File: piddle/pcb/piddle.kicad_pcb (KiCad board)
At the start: 2 copper layers, 139.2 x 138.5 mm, 88 parts, among them J1 Conn_01x03_Socket, J10 Conn_01x03_Socket, J11 Conn_01x03_Socket, J12 Conn_01x03_Socket, J13 Conn_01x03_Socket, J14 Conn_01x03_Socket, J15 Conn_01x03_Socket, J16 infrared receiver, J17 5v, J18 3v3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

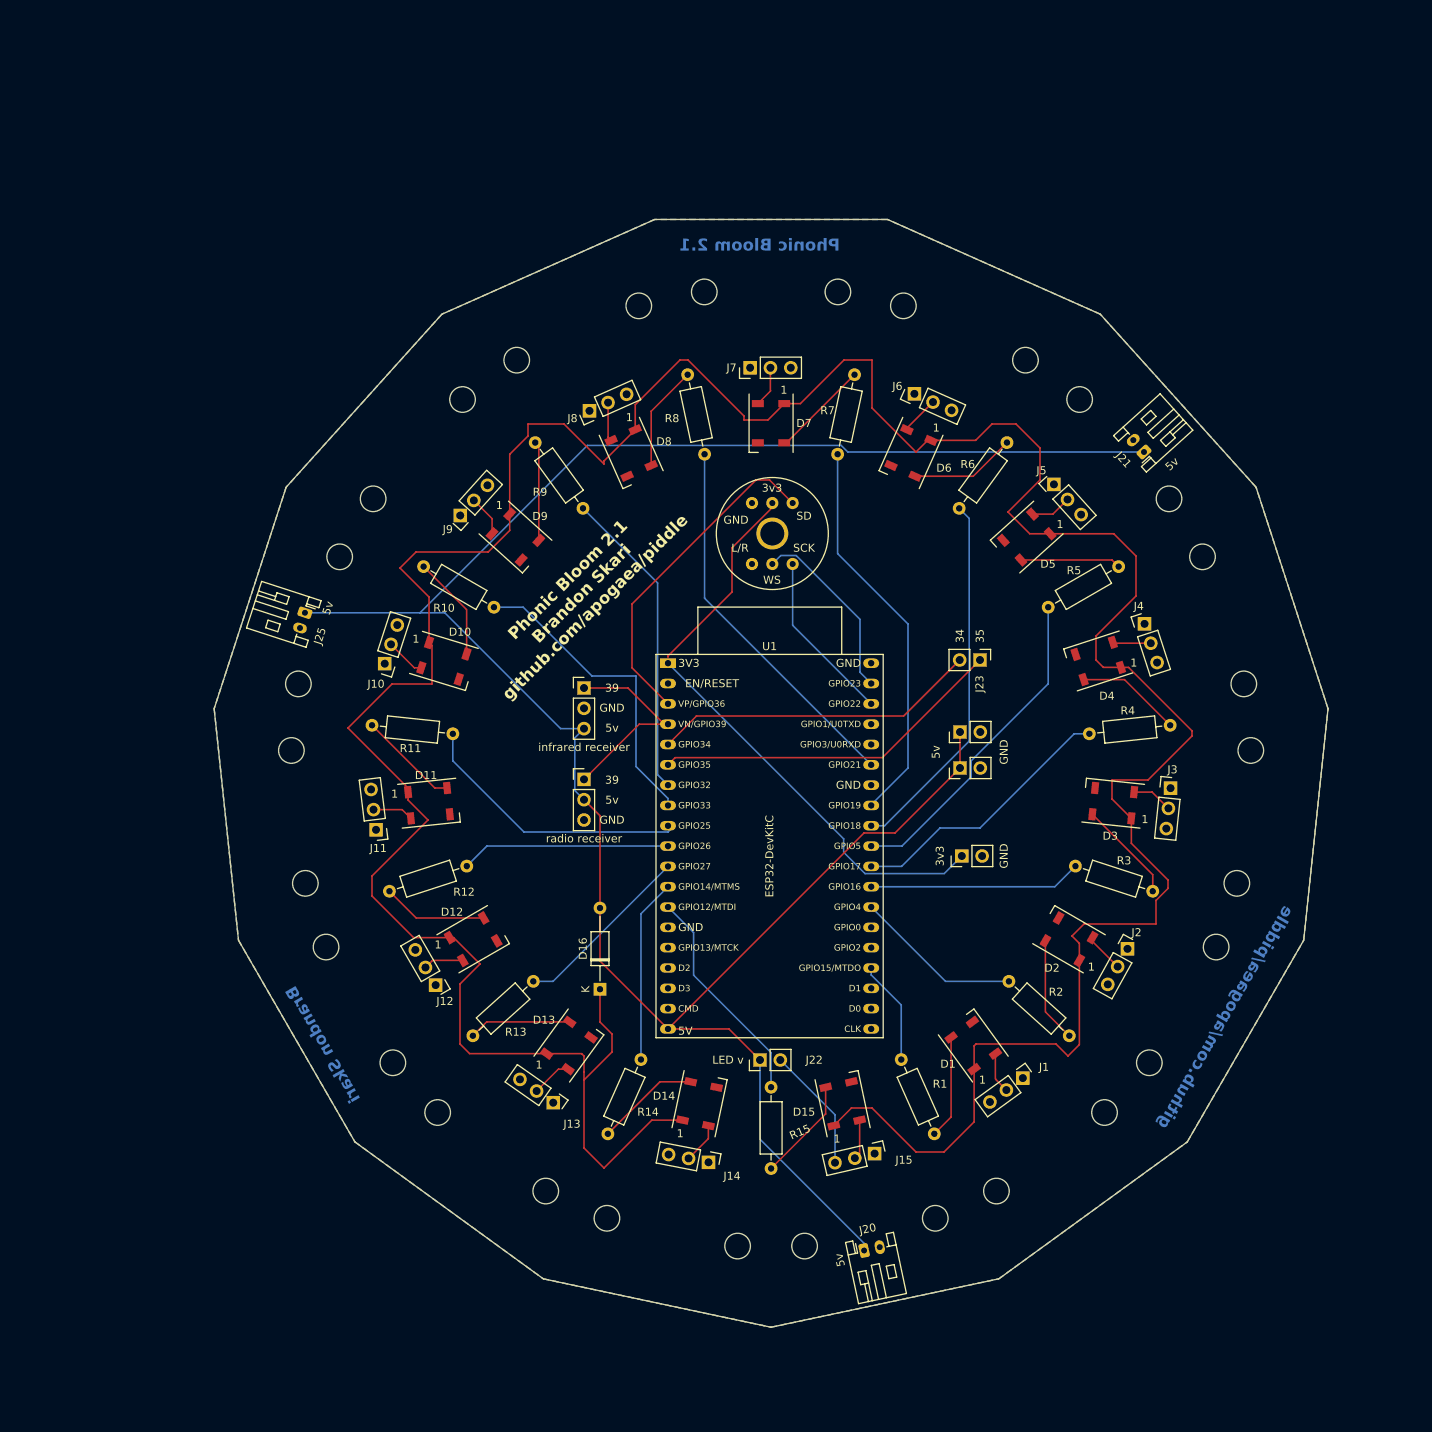
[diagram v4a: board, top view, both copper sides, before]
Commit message: Simplify and don't rearrange zones
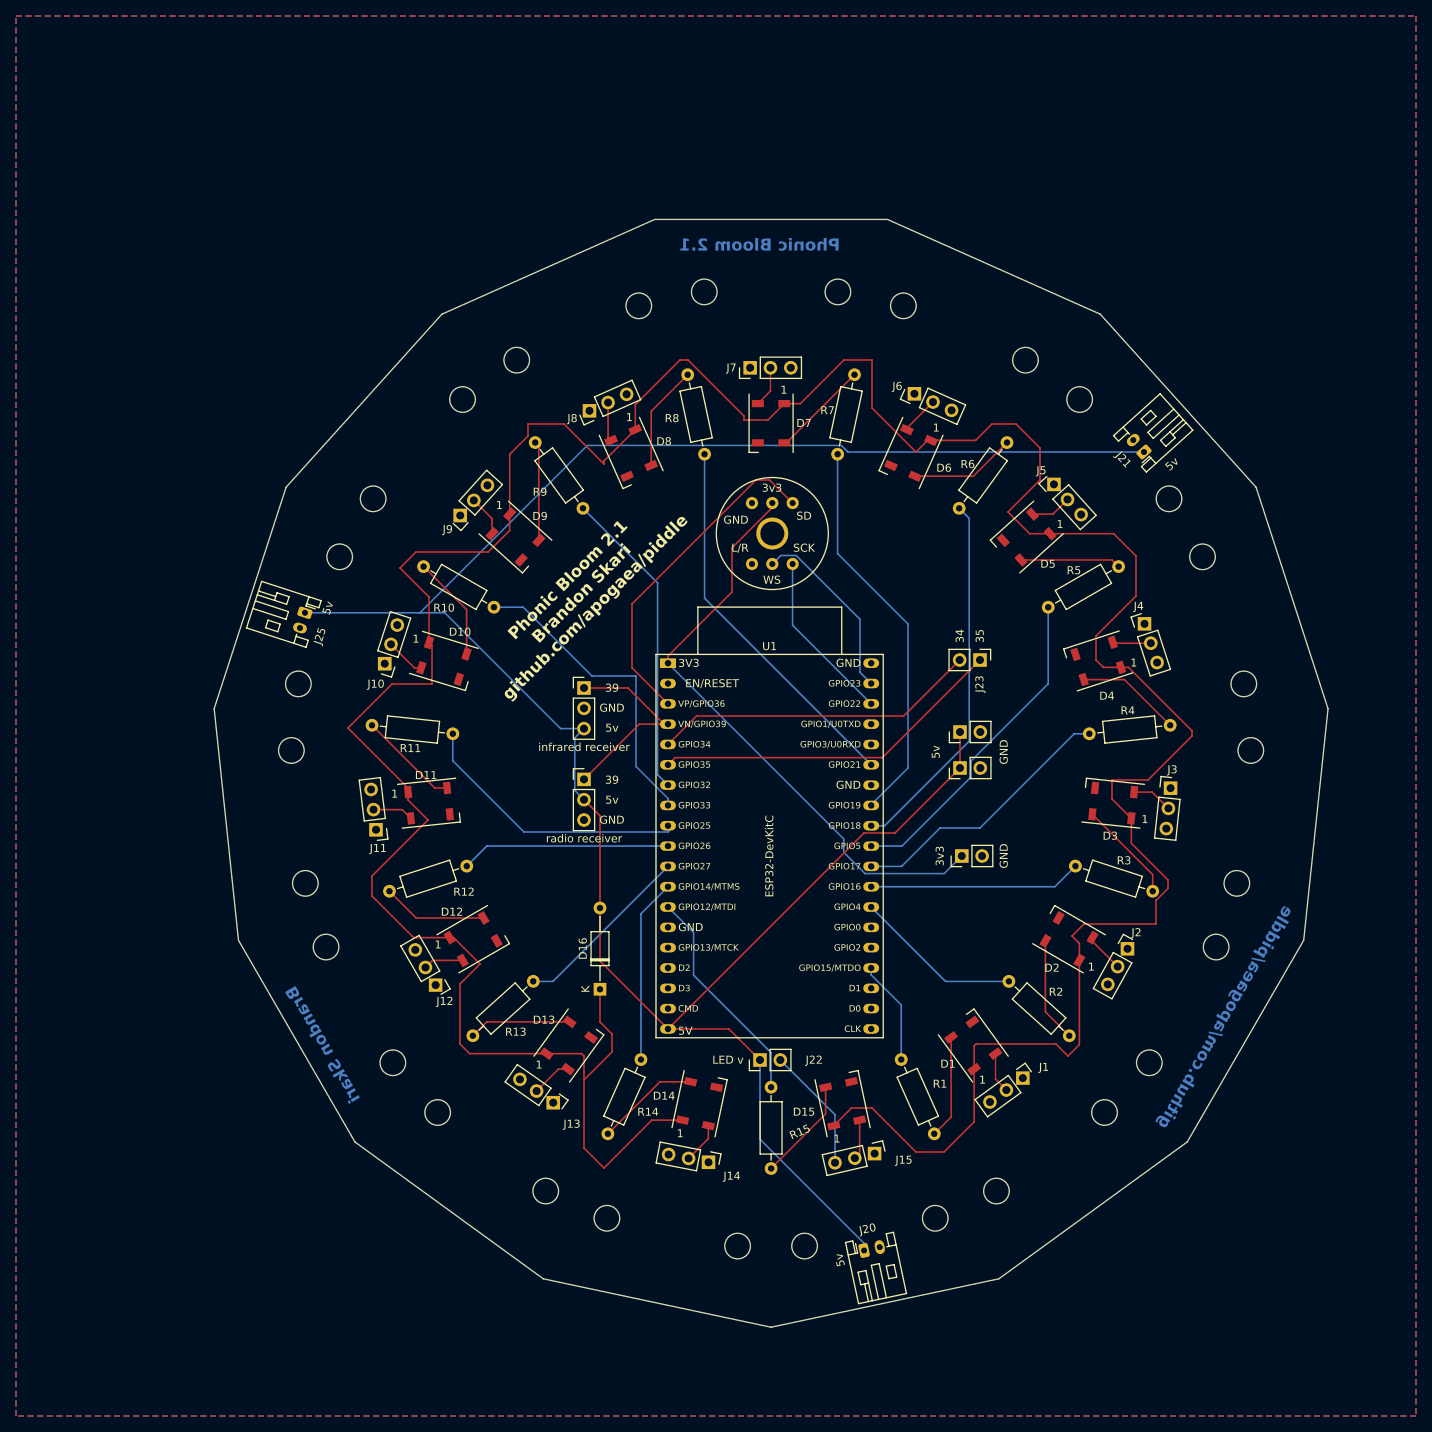
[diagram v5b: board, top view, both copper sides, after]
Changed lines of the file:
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@@
 		(polygon
 			(pts
-				(xy 100 170) (xy 128.4716 163.9482) (xy 152.0201 146.8391) (xy 166.574 121.6312) (xy 169.6165 92.683)
-				(xy 160.6218 65) (xy 141.145 43.3688) (xy 114.5538 31.5297) (xy 85.4462 31.5297) (xy 58.855 43.3688)
-				(xy 39.3782 65) (xy 30.3835 92.683) (xy 33.426 121.6312) (xy 47.9799 146.8391) (xy 71.5284 163.9482)
+				(xy 5.61328 6.096343) (xy 180.61328 6.096343) (xy 180.61328 181.096343) (xy 5.61328 181.096343)
 			)
 		)
-	)
-	(zone
-		(net 1)
-		(net_name "GND")
-		(layer "B.Cu")
-		(hatch edge 0.5)
-		(priority 1)
-		(connect_pads
-			(clearance 0.5)
-		)
-		(min_thickness 0.25)
-		(filled_areas_thickness no)
-		(fill yes
-			(thermal_gap 0.5)
-			(thermal_bridge_width 0.5)
-		)
-		(polygon
-			(pts
-				(xy 100 170) (xy 128.4716 163.9482) (xy 152.0201 146.8391) (xy 166.574 121.6312) (xy 169.6165 92.683)
-				(xy 160.6218 65) (xy 141.145 43.3688) (xy 114.5538 31.5297) (xy 85.4462 31.5297) (xy 58.855 43.3688)
-				(xy 39.3782 65) (xy 30.3835 92.683) (xy 33.426 121.6312) (xy 47.9799 146.8391) (xy 71.5284 163.9482)
-			)
-		)

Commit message: Fillet the edges
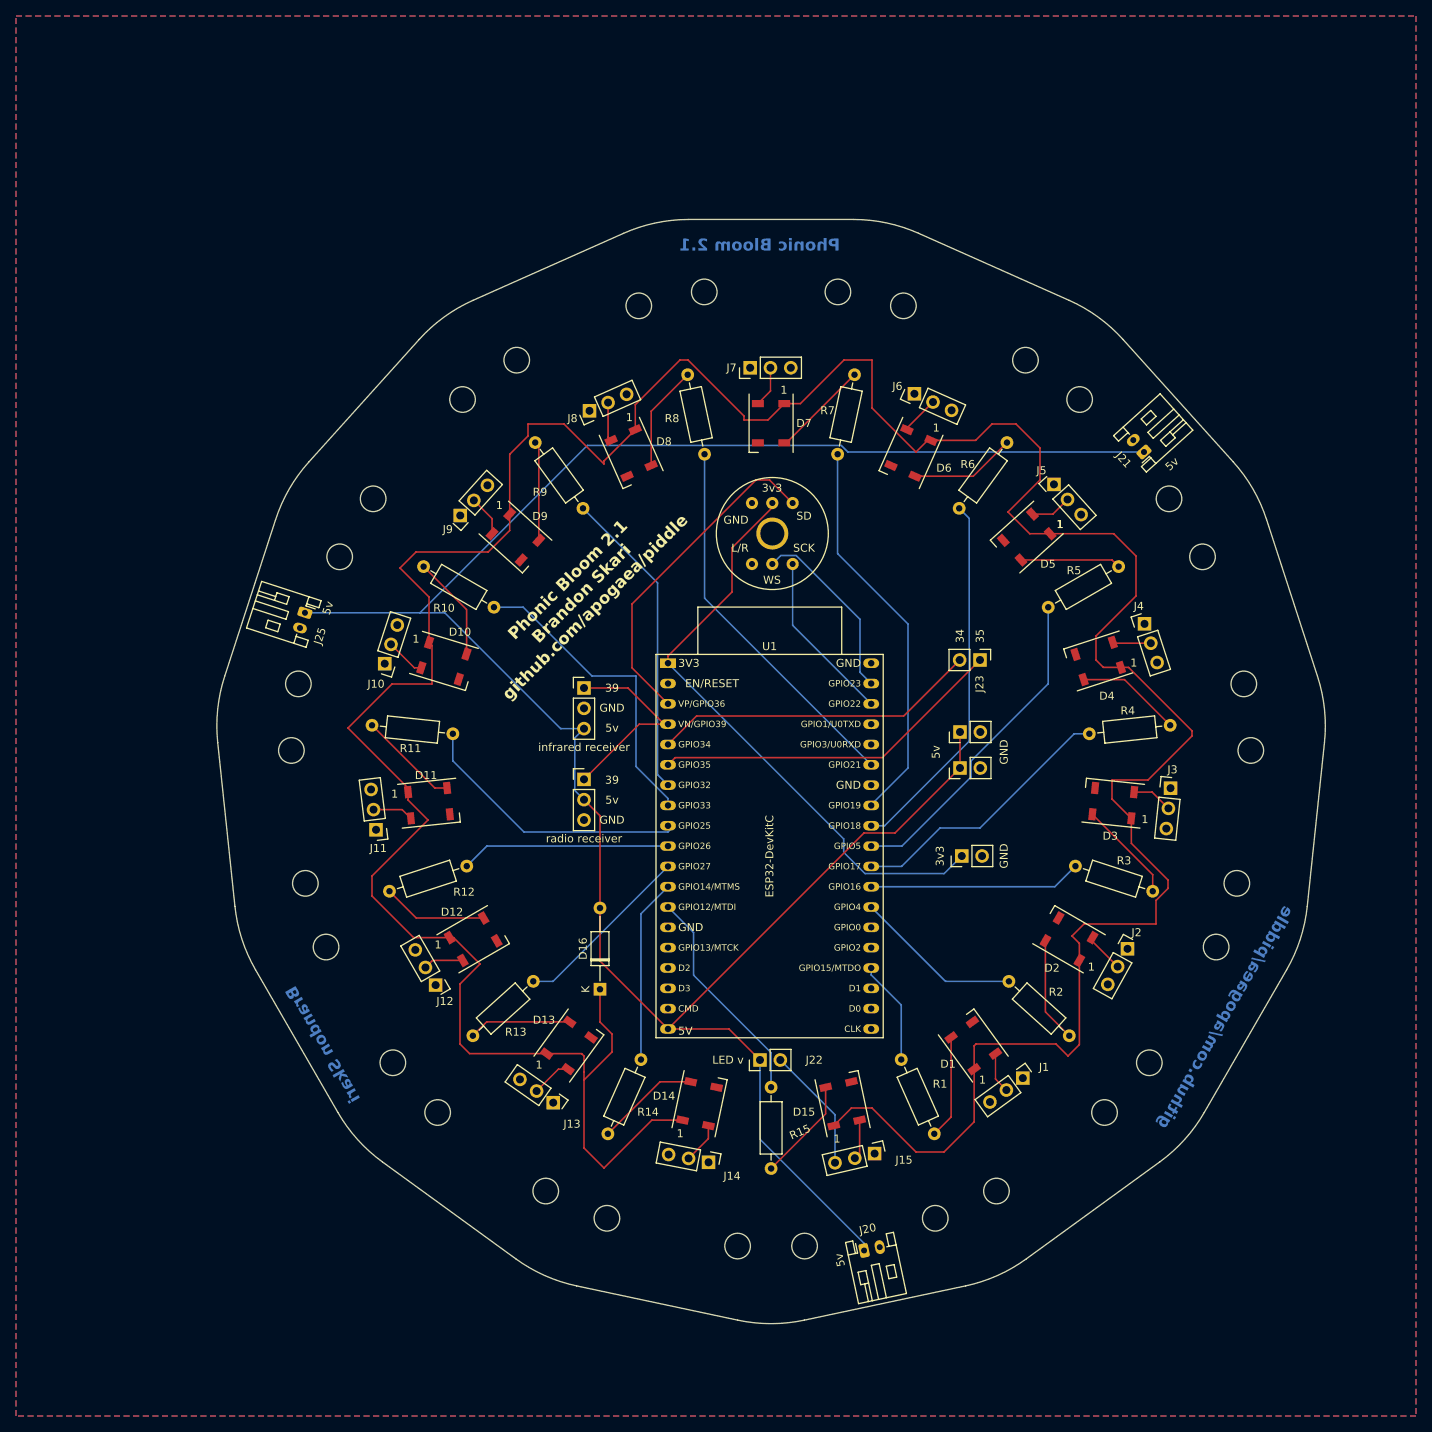
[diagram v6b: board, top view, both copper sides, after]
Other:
- board size 139.2 x 138.5 mm -> 138.6 x 138 mm
- board text added: "${REFERENCE}"
- board text added: "1"
